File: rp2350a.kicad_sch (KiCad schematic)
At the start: 43 parts, among them Q7 DMN1150UFB-7B, SW1 B3U-1000P, U11 RP2350A_C42411118, U12 ABM8-272-T3_C20625731, U13 W25Q32RVXHJQ TR

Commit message: almost finished routing
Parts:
- removed C108: 100nF, Capacitor_SMD:C_0402_1005Metric, symbol Device:C
- removed R40, R51: 10k, Resistor_SMD:R_0402_1005Metric, symbol Device:R
- removed R43, R49: 1k, Resistor_SMD:R_0402_1005Metric, symbol Device:R
- removed SW1: B3U-1000P, lib:KEY-SMD_B3U-1000PM, symbol lib:B3U-1000P
- added C2: 100n, Capacitor_SMD:C_0402_1005Metric, symbol Device:C
- added R10, R11, R12: 10k, Resistor_SMD:R_0402_1005Metric, symbol Device:R
- added R13: 1k, Resistor_SMD:R_0402_1005Metric, symbol Device:R
- added U21: TS2306A 240GF MSM 9_C2976675, lib:SW-SMD_4P-L3.0-W2.0-P0.85-LS3.5, symbol lib:TS2306A240GFMSM9_C2976675
- R1, R2, R44, R45: LCSC (none) -> C105872
- R39: LCSC (none) -> C25105
- R41: LCSC (none) -> C25087
- R42: LCSC (none) -> C106235
- R5, R50: LCSC (none) -> C60491
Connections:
- net +3.3V: now also R10.1
- net BEEPER: now also R13.1
- net GND: now also C2.2, R11.1, R12.1
- net VBAT_ADC: now also C2.1, R11.2
- net at U11.26 (RUN): now also R10.2
- net at Q7.1 (G), R5.2: now also R13.2
- net at U11.60 (QSPI_SS), U13.1 (/CS): now also U21.2
- net ESP8285_RST renamed ESP_BOOT0
- new net: R12.2, U21.1

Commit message: fixed gyro power and rp2350 inductor
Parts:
- removed L5: FTC160808S3R3MBCA, lib:IND-SMD_PSTMAA160808-4R7MB, symbol lib:FTC160808S3R3MBCA
- added L1: AOTA-B201610S3R3-101-T, lib:IND-SMD_L2.0-W1.6_AOTA-B201610S3R3-101-T, symbol lib:AOTA-B201610S3R3-101-T
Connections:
- net +1.1V: now also L1.1
- net at U11.48 (VREG_LX): now also L1.2
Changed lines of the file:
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@@
 	(wire
 		(pts
-			(xy 217.17 97.79) (xy 217.17 91.44)
-		)
-		(stroke
-			(width 0)
-			(type default)
-		)
-	)
-	(wire
-		(pts
 			(xy 193.04 203.2) (xy 199.39 203.2)
 		)
@@
 	(wire
 		(pts
-			(xy 217.17 81.28) (xy 217.17 77.47)
-		)
-		(stroke
-			(width 0)
-			(type default)
-		)
-	)
-	(wire
-		(pts
 			(xy 87.63 115.57) (xy 87.63 114.3)
 		)
@@
 	(wire
 		(pts
+			(xy 217.17 77.47) (xy 217.17 81.28)
+		)
+		(stroke
+			(width 0)
+			(type default)
+		)
+	)
+	(wire
+		(pts
 			(xy 109.22 60.96) (xy 109.22 64.77)
 		)
@@
 	(wire
 		(pts
+			(xy 217.17 91.44) (xy 217.17 97.79)
+		)
+		(stroke
+			(width 0)
+			(type default)
+		)
+	)
+	(wire
+		(pts
 			(xy 255.27 81.28) (xy 255.27 73.66)
 		)
@@
 	)
 	(symbol
+		(lib_id "lib:AOTA-B201610S3R3-101-T")
+		(at 217.17 86.36 270)
+		(unit 1)
+		(exclude_from_sim no)
+		(in_bom yes)
+		(on_board yes)
+		(dnp no)
+		(fields_autoplaced yes)
+		(property "Reference" "L1"
+			(at 219.71 85.7229 90)
+			(effects
+				(font
+					(size 1.27 1.27)
+				)
+				(justify left)
+			)
+		)
+		(property "Value" "AOTA-B201610S3R3-101-T"
+			(at 219.71 88.2629 90)
+			(effects
+				(font
+					(size 1.27 1.27)
+				)
+				(justify left)
+			)
+		)
+		(property "Footprint" "lib:IND-SMD_L2.0-W1.6_AOTA-B201610S3R3-101-T"
+			(at 209.55 86.36 0)
+			(effects
+				(font
+					(size 1.27 1.27)
+				)
+				(hide yes)
+			)
+		)
+		(property "Datasheet" ""
+			(at 217.17 86.36 0)
+			(effects
+				(font
+					(size 1.27 1.27)
+				)
+				(hide yes)
+			)
+		)
+		(property "Description" ""
+			(at 217.17 86.36 0)
+			(effects
+				(font
+					(size 1.27 1.27)
+				)
+				(hide yes)
+			)
+		)
+		(property "LCSC Part" "C42411119"
+			(at 207.01 86.36 0)
+			(effects
+				(font
+					(size 1.27 1.27)
+				)
+				(hide yes)
+			)
+		)
+		(pin "1"
+		)
+		(pin "2"
+		)
+		(instances
+			(project ""
+				(path "/fb88b6f9-ee39-4640-a9d4-04a17ceeac64/cec45a0d-1d48-4800-9760-14c521e5fc8b"
+					(reference "L1")
+					(unit 1)
+				)
+			)
+		)
+	)
+	(symbol
 		(lib_id "power:GND")
 		(at 48.26 191.77 270)
@@
 					(unit 1)
 				)
-			)
-		)
-	)
-	(symbol
-		(lib_id "lib:FTC160808S3R3MBCA")
-		(at 217.17 86.36 90)
-		(unit 1)
-		(exclude_from_sim no)
-		(in_bom yes)
-		(on_board yes)
-		(dnp no)
-		(fields_autoplaced yes)
-		(property "Reference" "L5"
-			(at 218.44 85.0899 90)
-			(effects
-				(font
-					(size 1.27 1.27)
-				)
-				(justify right)
-			)
-		)
-		(property "Value" "FTC160808S3R3MBCA"
-			(at 218.44 87.6299 90)
-			(effects
-				(font
-					(size 1.27 1.27)
-				)
-				(justify right)
-			)
-		)
-		(property "Footprint" "lib:IND-SMD_PSTMAA160808-4R7MB"
-			(at 224.79 86.36 0)
-			(effects
-				(font
-					(size 1.27 1.27)
-				)
-				(hide yes)
-			)
-		)
-		(property "Datasheet" ""
-			(at 217.17 86.36 0)
-			(effects
-				(font
-					(size 1.27 1.27)
-				)
-				(hide yes)
-			)
-		)
-		(property "Description" ""
-			(at 217.17 86.36 0)
-			(effects
-				(font
-					(size 1.27 1.27)
-				)
-				(hide yes)
-			)
-		)
-		(property "LCSC Part" "C46594346"
-			(at 227.33 86.36 0)
-			(effects
-				(font
-					(size 1.27 1.27)
-				)
-				(hide yes)
-			)
-		)
-		(pin "1"
-		)
-		(pin "2"
-		)
-		(instances
-			(project ""
-				(path "/fb88b6f9-ee39-4640-a9d4-04a17ceeac64/cec45a0d-1d48-4800-9760-14c521e5fc8b"
-					(reference "L5")
-					(unit 1)
-				)

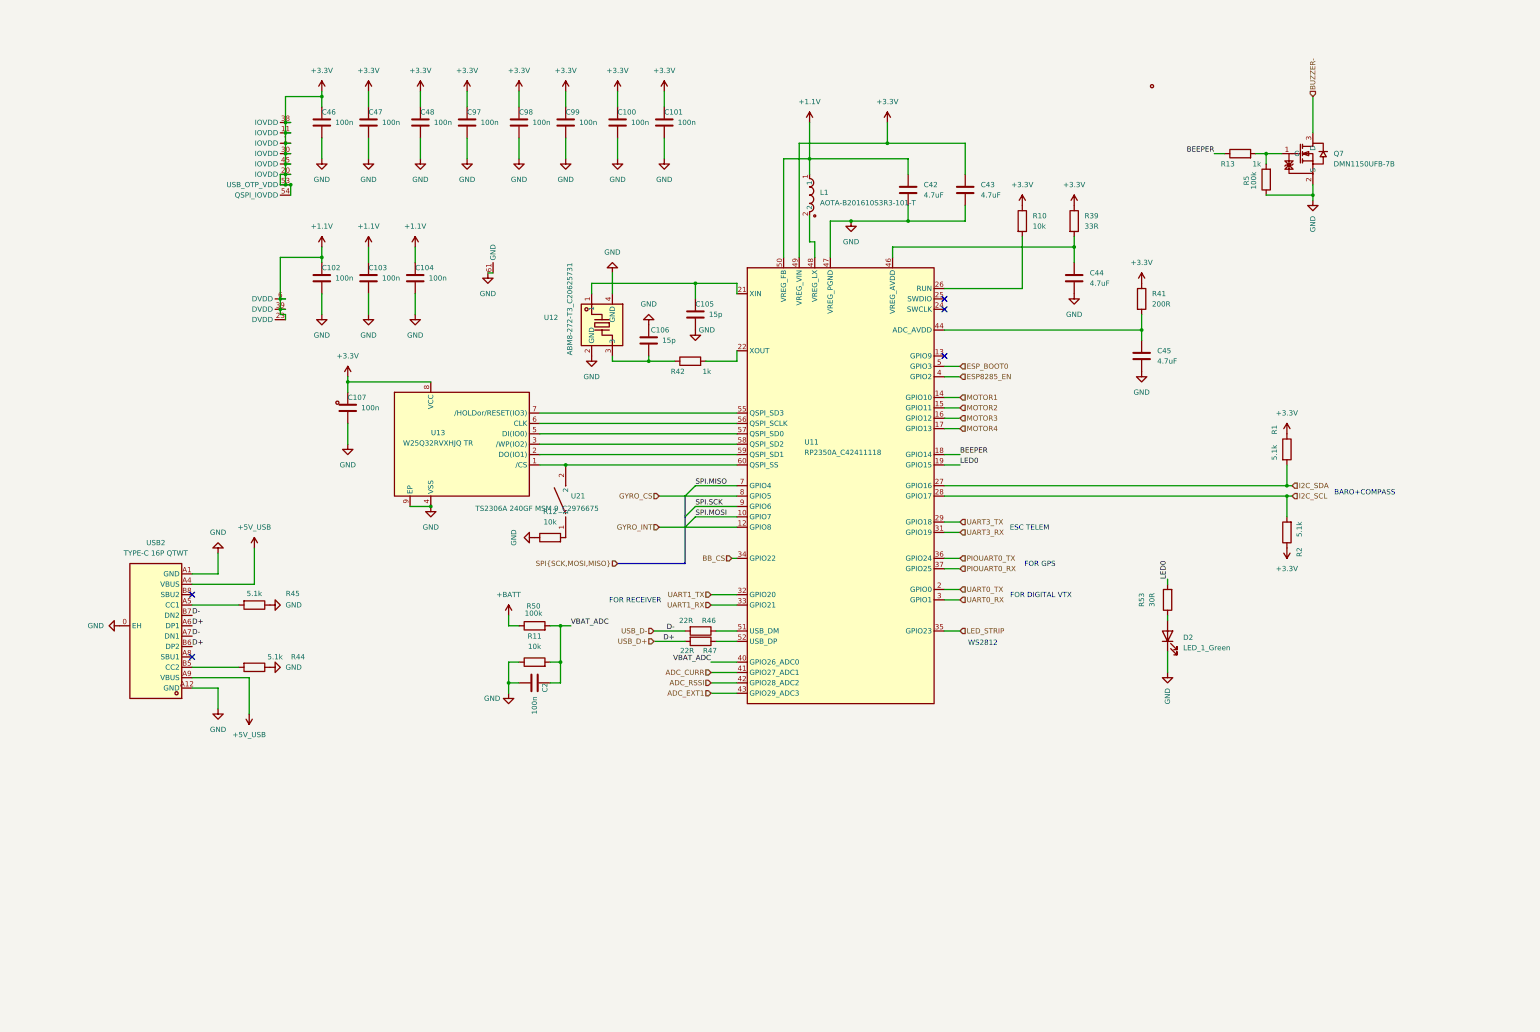
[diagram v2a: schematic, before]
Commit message: Switched to RP2354A and re-routed
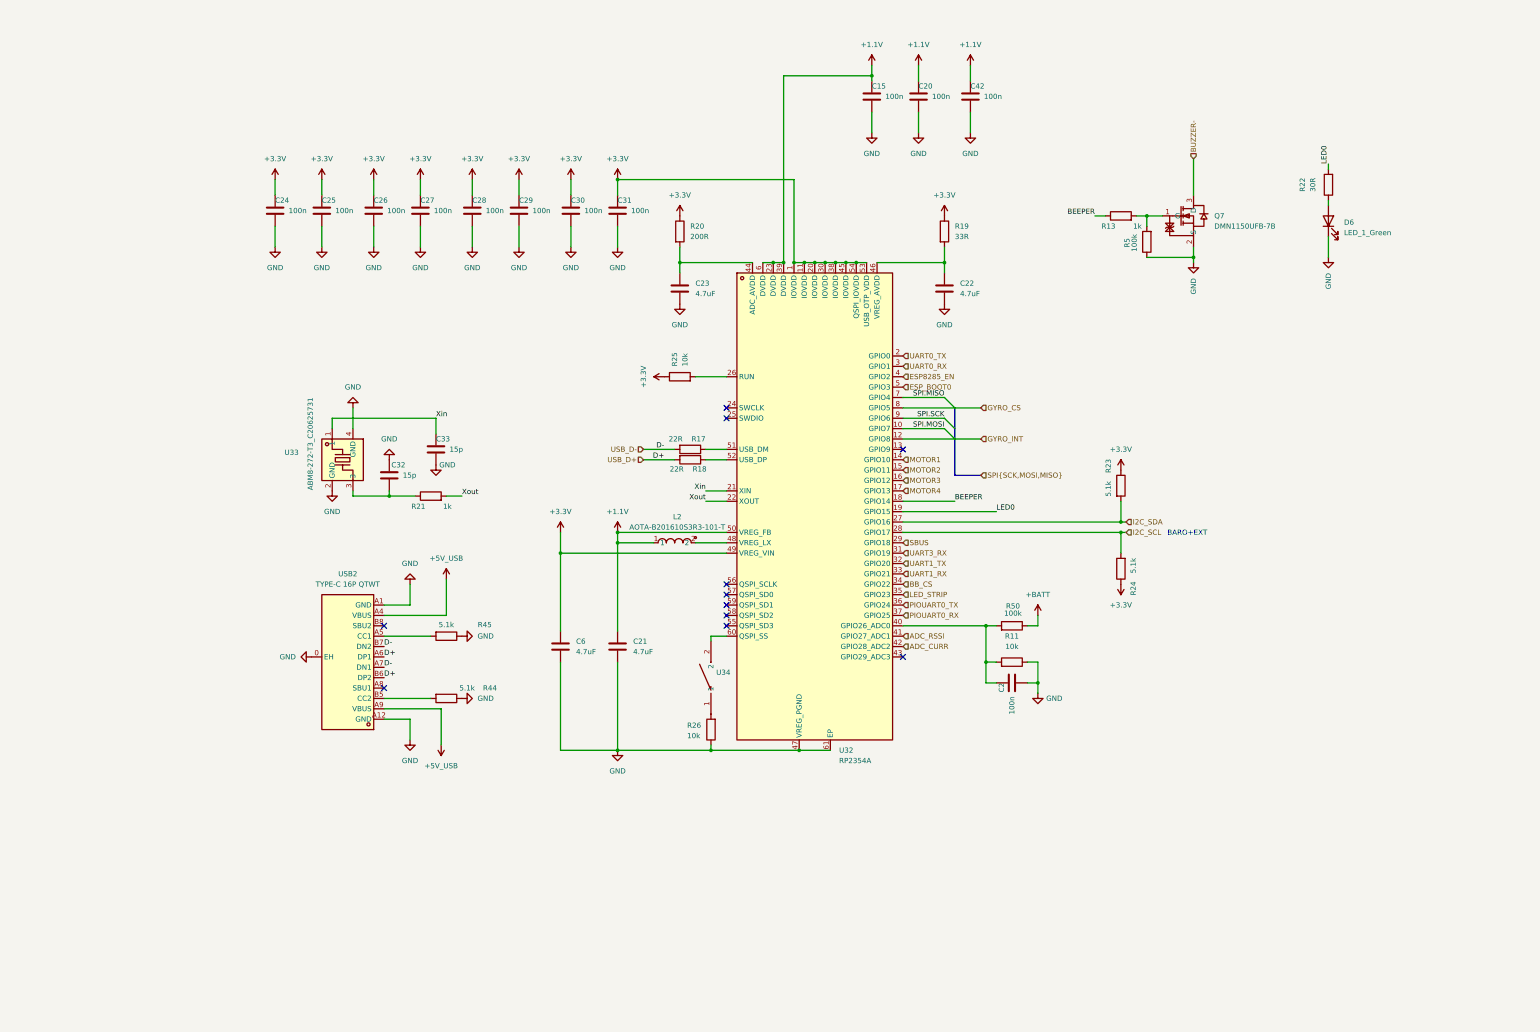
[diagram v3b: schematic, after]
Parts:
- removed C100, C101, C102, C103, C104, C107, C46, C47, C48, C97, C98, C99: 100n, Capacitor_SMD:C_0402_1005Metric, symbol Device:C
- removed C105, C106: 15p, Capacitor_SMD:C_0402_1005Metric, symbol Device:C
- removed C43, C44, C45: 4.7uF, Capacitor_SMD:C_0402_1005Metric, symbol Device:C
- removed D2: LED_1_Green, LED_SMD:LED_0603_1608Metric, symbol Device:LED
- removed L1: AOTA-B201610S3R3-101-T, lib:IND-SMD_L2.0-W1.6_AOTA-B201610S3R3-101-T, symbol lib:AOTA-B201610S3R3-101-T
- removed R1, R2: 5.1k, Resistor_SMD:R_0402_1005Metric, symbol Device:R
- removed R10, R12: 10k, Resistor_SMD:R_0402_1005Metric, symbol Device:R
- removed R39: 33R, Resistor_SMD:R_0402_1005Metric, symbol Device:R
- removed R41: 200R, Resistor_SMD:R_0402_1005Metric, symbol Device:R
- removed R42: 1k, Resistor_SMD:R_0402_1005Metric, symbol Device:R
- removed R46, R47: 22R, Resistor_SMD:R_0402_1005Metric, symbol Device:R
- removed R53: 30R, Resistor_SMD:R_0402_1005Metric, symbol Device:R
- removed U11: RP2350A_C42411118, lib:QFN-60_L7.0-W7.0-P0.40-TL-EP3.4, symbol lib:RP2350A_C42411118
- removed U12: ABM8-272-T3_C20625731, lib:CRYSTAL-SMD_4P-L3.2-W2.5-BL, symbol lib:ABM8-272-T3_C20625731
- removed U13: W25Q32RVXHJQ TR, lib:USON-8_L3.0-W2.0-P0.50-BL-EP, symbol lib:W25Q32RVXHJQTR
- removed U21: TS2306A 240GF MSM 9_C2976675, lib:SW-SMD_4P-L3.0-W2.0-P0.85-LS3.5, symbol lib:TS2306A240GFMSM9_C2976675
- added C15, C20, C24, C25, C26, C27, C28, C29, C30, C31: 100n, Capacitor_SMD:C_0402_1005Metric, symbol Device:C
- added C21, C22, C23, C6: 4.7uF, Capacitor_SMD:C_0402_1005Metric, symbol Device:C
- added C32, C33: 15p, Capacitor_SMD:C_0402_1005Metric, symbol Device:C
- added D6: LED_1_Green, LED_SMD:LED_0603_1608Metric, symbol Device:LED
- added L2: AOTA-B201610S3R3-101-T, lib:IND-SMD_L2.0-W1.6_AOTA-B201610S3R3-101-T, symbol lib:AOTA-B201610S3R3-101-T
- added R17, R18: 22R, Resistor_SMD:R_0402_1005Metric, symbol Device:R
- added R19: 33R, Resistor_SMD:R_0402_1005Metric, symbol Device:R
- added R20: 200R, Resistor_SMD:R_0402_1005Metric, symbol Device:R
- added R21: 1k, Resistor_SMD:R_0402_1005Metric, symbol Device:R
- added R22: 30R, Resistor_SMD:R_0402_1005Metric, symbol Device:R
- added R23, R24: 5.1k, Resistor_SMD:R_0402_1005Metric, symbol Device:R
- added R25, R26: 10k, Resistor_SMD:R_0402_1005Metric, symbol Device:R
- added U32: RP2354A, lib:QFN-60_L7.0-W7.0-P0.40-TL-EP3.4, symbol lib:RP2354A
- added U33: ABM8-272-T3_C20625731, lib:CRYSTAL-SMD_4P-L3.2-W2.5-BL, symbol lib:ABM8-272-T3_C20625731
- added U34: TS2306A 240GF MSM 9_C2976675, lib:SW-SMD_4P-L3.0-W2.0-P0.85-LS3.5, symbol lib:TS2306A240GFMSM9_C2976675
- C42: value 4.7uF -> 100n; LCSC C23733 -> C1525
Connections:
- net +1.1V: now also C15.1, C20.1, C21.1, L2.1, U32.23 (DVDD), U32.39 (DVDD), U32.50 (VREG_FB), U32.6 (DVDD)
- net +3.3V: now also C24.1, C25.1, C26.1, C27.1, C28.1, C29.1, C30.1, C31.1, C6.1, R19.1, R20.1, R23.1, R24.1, R25.1, U32.1 (IOVDD), U32.11 (IOVDD), U32.20 (IOVDD), U32.30 (IOVDD), U32.38 (IOVDD), U32.45 (IOVDD), U32.49 (VREG_VIN), U32.53 (USB_OTP_VDD), U32.54 (QSPI_IOVDD)
- net ADC_CURR: now also U32.42 (GPIO28_ADC2)
- net ADC_RSSI: now also U32.41 (GPIO27_ADC1)
- net BB_CS: now also U32.34 (GPIO22)
- net BEEPER: now also U32.18 (GPIO14)
- net ESP8285_EN: now also U32.4 (GPIO2)
- net ESP_BOOT0: now also U32.5 (GPIO3)
- net GND: now also C15.2, C20.2, C21.2, C22.2, C23.2, C24.2, C25.2, C26.2, C27.2, C28.2, C29.2, C30.2, C31.2, C32.1, C33.2, C6.2, D6.1 (K), R26.1, U32.47 (VREG_PGND), U32.61 (EP), U33.2 (GND), U33.4 (GND)
- net GYRO_CS: now also U32.8 (GPIO5)
- net GYRO_INT: now also U32.12 (GPIO8)
- net I2C_SCL: now also R24.2, U32.28 (GPIO17)
- net I2C_SDA: now also R23.2, U32.27 (GPIO16)
- net LED0: now also R22.2, U32.19 (GPIO15)
- net LED_STRIP: now also U32.35 (GPIO23)
- net MOTOR1: now also U32.14 (GPIO10)
- net MOTOR2: now also U32.15 (GPIO11)
- net MOTOR3: now also U32.16 (GPIO12)
- net MOTOR4: now also U32.17 (GPIO13)
- net PIOUART0_RX: now also U32.37 (GPIO25)
- net PIOUART0_TX: now also U32.36 (GPIO24)
- net SPI.MISO: now also U32.7 (GPIO4)
- net SPI.MOSI: now also U32.10 (GPIO7)
- net SPI.SCK: now also U32.9 (GPIO6)
- net UART0_RX: now also U32.3 (GPIO1)
- net UART0_TX: now also U32.2 (GPIO0)
- net UART1_RX: now also U32.33 (GPIO21)
- net UART1_TX: now also U32.32 (GPIO20)
- net UART3_RX: now also U32.31 (GPIO19)
- net USB_D+: now also R18.2
- net USB_D-: now also R17.2
- net VBAT_ADC: no longer names the net of C2.1, R11.2, R50.2
- net VBAT_ADC: now also U32.40 (GPIO26_ADC0)
- new net: C32.2, R21.1, U33.3
- new net: C22.1, R19.2, U32.46 (VREG_AVDD)
- new net: C23.1, R20.2, U32.44 (ADC_AVDD)
- new net: R25.2, U32.26 (RUN)
- new net: L2.2, U32.48 (VREG_LX)
- new net: R26.2, U34.1
- new net: U32.60 (QSPI_SS), U34.2
- new net: D6.2 (A), R22.1
- new net: R17.1, U32.51 (USB_DM)
- new net: R18.1, U32.52 (USB_DP)
- new net SBUS: U32.29 (GPIO18)
- new net Xin: C33.1, U32.21 (XIN), U33.1
- new net Xout: R21.2, U32.22 (XOUT)
- no-connect marks 5 -> 11
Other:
- note added: "BARO+EXT"
- note removed: "BARO+COMPASS"
- note removed: "ESC TELEM"
- note removed: "FOR DIGITAL VTX"
- note removed: "FOR GPS"
- note removed: "FOR RECEIVER"
- note removed: "WS2812"
- moved on the sheet: C2, Q7, R11, R13, R44, R45, R5, R50, USB2

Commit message: Added Open-OSD-X and new layout
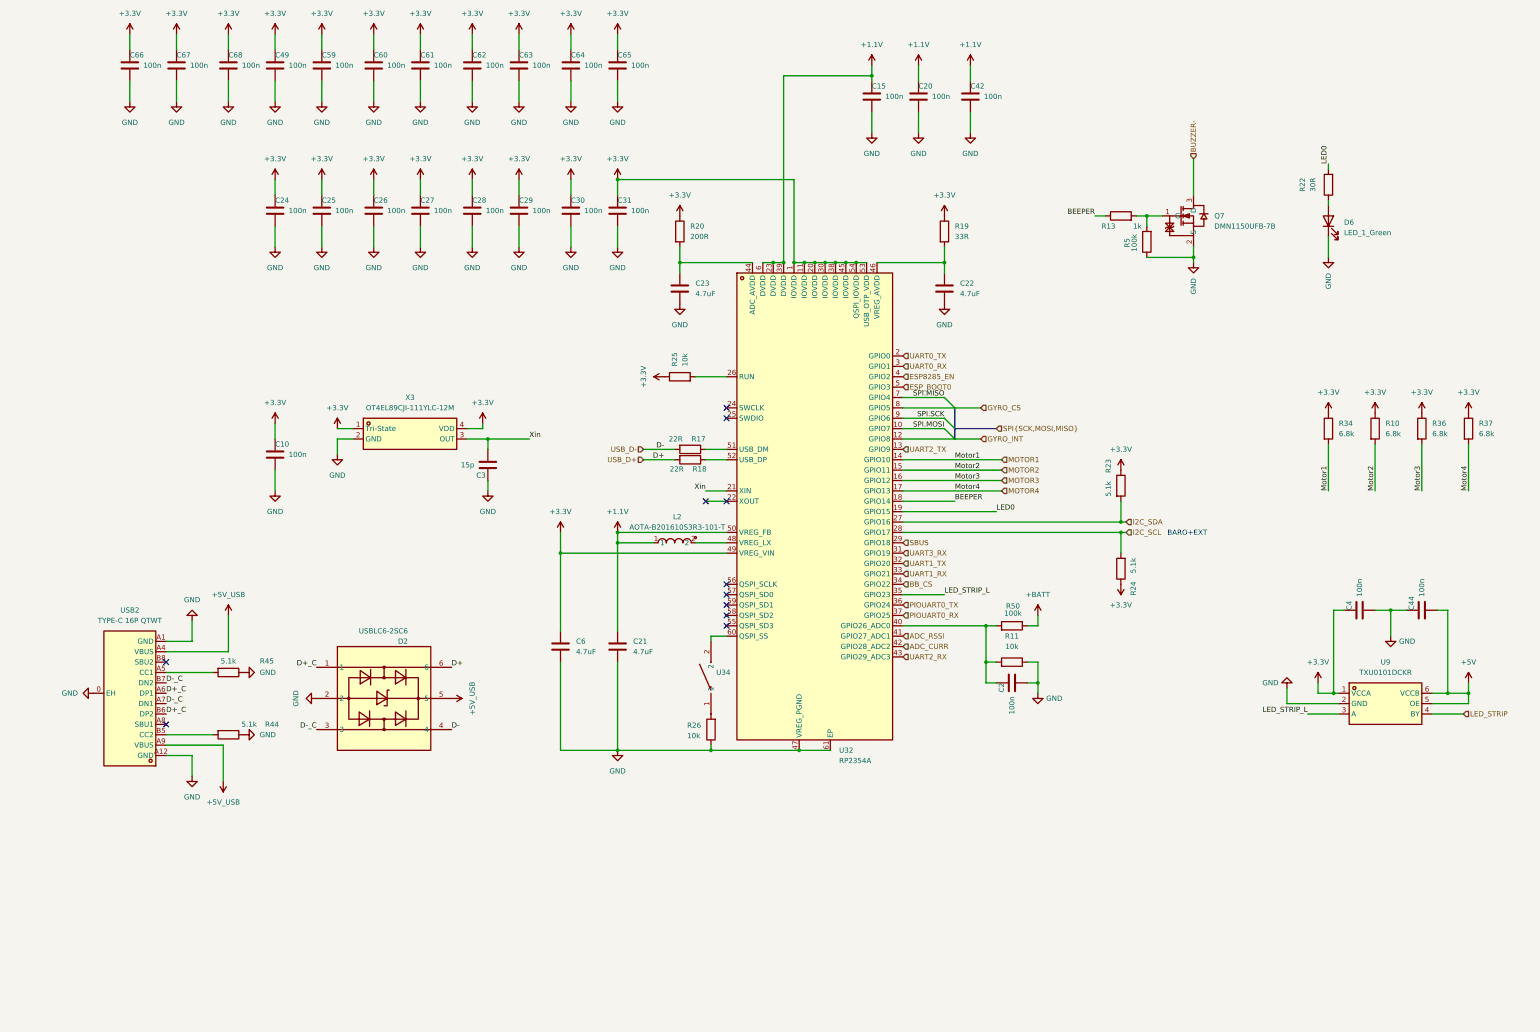
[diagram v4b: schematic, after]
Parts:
- removed C32, C33: 15p, Capacitor_SMD:C_0402_1005Metric, symbol Device:C
- removed R21: 1k, Resistor_SMD:R_0402_1005Metric, symbol Device:R
- removed U33: ABM8-272-T3_C20625731, lib:CRYSTAL-SMD_4P-L3.2-W2.5-BL, symbol lib:ABM8-272-T3_C20625731
- added C10, C4, C44, C49, C59, C60, C61, C62, C63, C64, C65, C66, C67, C68: 100n, Capacitor_SMD:C_0402_1005Metric, symbol Device:C
- added C3: 15p, Capacitor_SMD:C_0402_1005Metric, symbol Device:C
- added D2: USBLC6-2SC6, lib:SOT-23-6_L2.9-W1.6-P0.95-LS2.8-BL, symbol lib:USBLC6-2SC6
- added R10, R34, R36, R37: 6.8k, Resistor_SMD:R_0402_1005Metric, symbol Device:R
- added U9: TXU0101DCKR, lib:SC-70-6_L2.0-W1.3-P0.65-LS2.1-BL, symbol lib:TXU0101DCKR
- added X3: OT4EL89CJI-111YLC-12M, lib:OSC-SMD_4P-L1.6-W1.2-BL-1, symbol lib:OT4EL89CJI-111YLC-12M
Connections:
- net +3.3V: now also C10.1, C4.1, C49.1, C59.1, C60.1, C61.1, C62.1, C63.1, C64.1, C65.1, C66.1, C67.1, C68.1, R10.1, R34.1, R36.1, R37.1, U9.1 (VCCA), X3.1 (Tri-State), X3.4 (VDD)
- net +5V_USB: now also D2.5
- net GND: now also C10.2, C3.1, C4.2, C44.1, C49.2, C59.2, C60.2, C61.2, C62.2, C63.2, C64.2, C65.2, C66.2, C67.2, C68.2, D2.2, U9.2 (GND), X3.2 (GND)
- net LED_STRIP: now also U9.4 (BY); no longer U32.35 (GPIO23)
- net MOTOR1: now also R34.2
- net MOTOR2: now also R10.2
- net MOTOR3: now also R36.2
- net MOTOR4: now also R37.2
- net USB_D+: now also D2.6; no longer USB2.A6 (DP1), USB2.B6 (DP2)
- net USB_D-: now also D2.4; no longer USB2.A7 (DN1), USB2.B7 (DN2)
- net Xin: now also C3.2, X3.3 (OUT)
- net UART2_TX: now reaches U32.13 (GPIO9)
- net UART2_RX: now reaches U32.43 (GPIO29_ADC3)
- net Xout: no longer names the net of U32.22 (XOUT)
- new net +5V: C44.2, U9.5 (OE), U9.6 (VCCB)
- new net D+_C: D2.1, USB2.A6 (DP1), USB2.B6 (DP2)
- new net D-_C: D2.3, USB2.A7 (DN1), USB2.B7 (DN2)
- new net LED_STRIP_L: U32.35 (GPIO23), U9.3 (A)
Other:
- moved on the sheet: R44, R45, USB2

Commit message: Ordered first revision
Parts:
- removed C49, C59, C60, C61, C62, C63, C64, C65, C66, C67, C68: 100n, Capacitor_SMD:C_0402_1005Metric, symbol Device:C
- D6: LCSC (none) -> C2994781
- R10, R34: LCSC (none) -> C2906876
- R17, R18: value 22R -> 30R; LCSC (none) -> C138007
- R19: value 33R -> 30R; LCSC C25105 -> C138007
- R22: LCSC (none) -> C138007
- R23: value 5.1k -> 6.8k
- R24: value 5.1k -> 6.8k; LCSC C105872 -> C2906876
